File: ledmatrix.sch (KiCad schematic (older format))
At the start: 51 parts, among them U58 sled1735

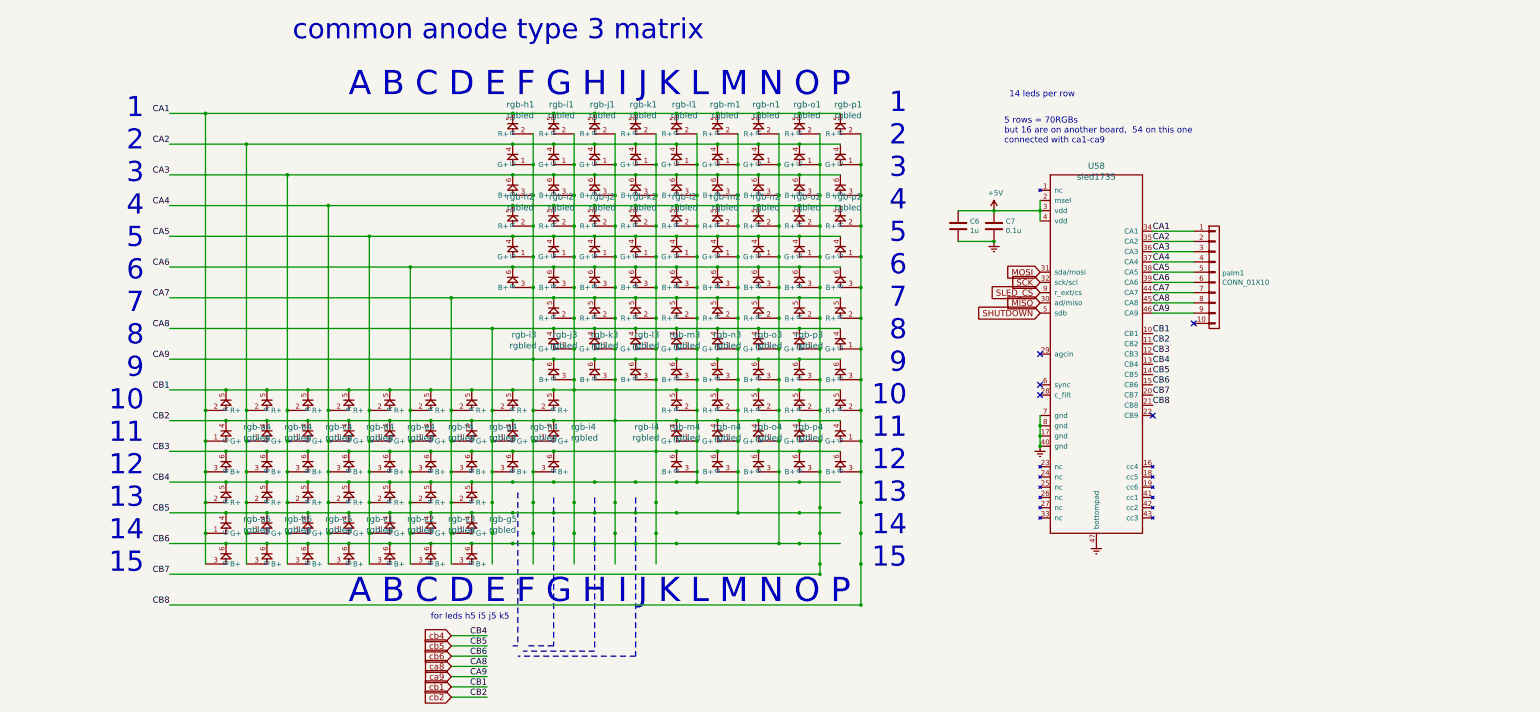
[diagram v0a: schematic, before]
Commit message: full BOM info on parts
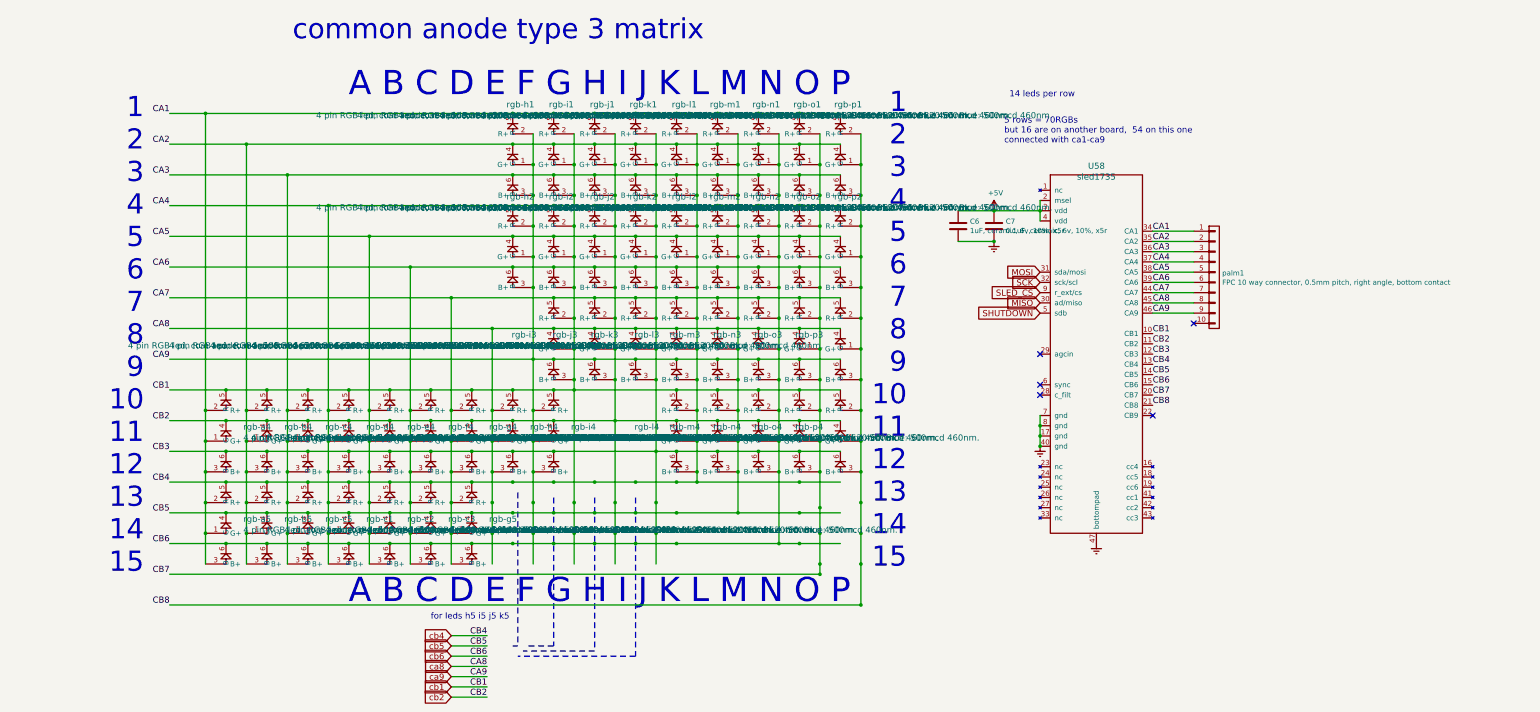
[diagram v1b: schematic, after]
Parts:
- C6: value 1u -> 1uF, ceramic, 6v, 10%, x5r; supplier (none) -> any/open
- C7: value 0.1u -> 0.1uF, ceramic, 6v, 10%, x5r; supplier (none) -> any/open
- U58: footprint fp:QFN-56_EP_4.5x6.5_Pitch0.4mm -> fp:QFN-46_EP_4.5x6.5_Pitch0.4mm; supplier (none) -> sonix; supplier PN (none) -> SLED1735
- palm1: value CONN_01X10 -> FPC 10 way connector, 0.5mm pitch, right angle, bottom contact; supplier (none) -> any/open
- rgb-a4, rgb-a5, rgb-b4, rgb-b5, rgb-c1, rgb-c2, rgb-c3, rgb-c4, rgb-c5, rgb-d4, rgb-e4, rgb-f4, rgb-g4, rgb-h1, rgb-h2, rgb-h4, rgb-i1, rgb-i2, rgb-i3, rgb-i4, rgb-j1, rgb-j2, rgb-j3, rgb-k1, rgb-k2, rgb-k3, rgb-l1, rgb-l2, rgb-l3, rgb-l4, rgb-m1, rgb-m2, rgb-m3, rgb-m4, rgb-n1, rgb-n2, rgb-n3, rgb-n4, rgb-o1, rgb-o2, rgb-o3, rgb-o4, rgb-p1, rgb-p2, rgb-p3, rgb-p4: value rgbled -> 4 pin RGB led, com anode, red: 500mcd 620nm. Green: 1000mcd 520nm. Blue: 500mcd 460nm.; supplier (none) -> any/open
- rgb-g5: value rgbled -> 4 pin RGB led, com anode, red: 500mcd 620nm. Green: 1000mcd 520nm. Blue: 500mcd 460nm.; MOQ (none) -> Value; leadtime (none) -> Value; supplier (none) -> any/open; supplier PN (none) -> Value

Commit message: changed fp name of sled and added the J to part number
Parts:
- U58: footprint fp:QFN-46_EP_4.5x6.5_Pitch0.4mm -> fp:QFN-56_EP_4.5x6.5_Pitch0.4mm; MOQ (none) -> Value; leadtime (none) -> Value; supplier PN SLED1735 -> SLED1735J
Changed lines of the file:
@@
 F 0 "U58" H 10050 2987 60  0000 C CNN
 F 1 "sled1735" H 10050 2881 60  0000 C CNN
-F 2 "fp:QFN-46_EP_4.5x6.5_Pitch0.4mm" H 9850 2250 60  0001 C CNN
+F 2 "fp:QFN-56_EP_4.5x6.5_Pitch0.4mm" H 9850 2250 60  0001 C CNN
 F 3 "" H 9850 2250 60  0001 C CNN
 F 4 "sonix" H 0   0   60  0001 C CNN "supplier"
-F 5 "SLED1735" H 0   0   60  0001 C CNN "supplier PN"
+F 5 "SLED1735J" H 0   0   60  0001 C CNN "supplier PN"
+F 6 "Value" H 9850 2250 60  0001 C CNN "MOQ"
+F 7 "Value" H 9850 2250 60  0001 C CNN "leadtime"
 	1    9850 2250
 	1    0    0    -1

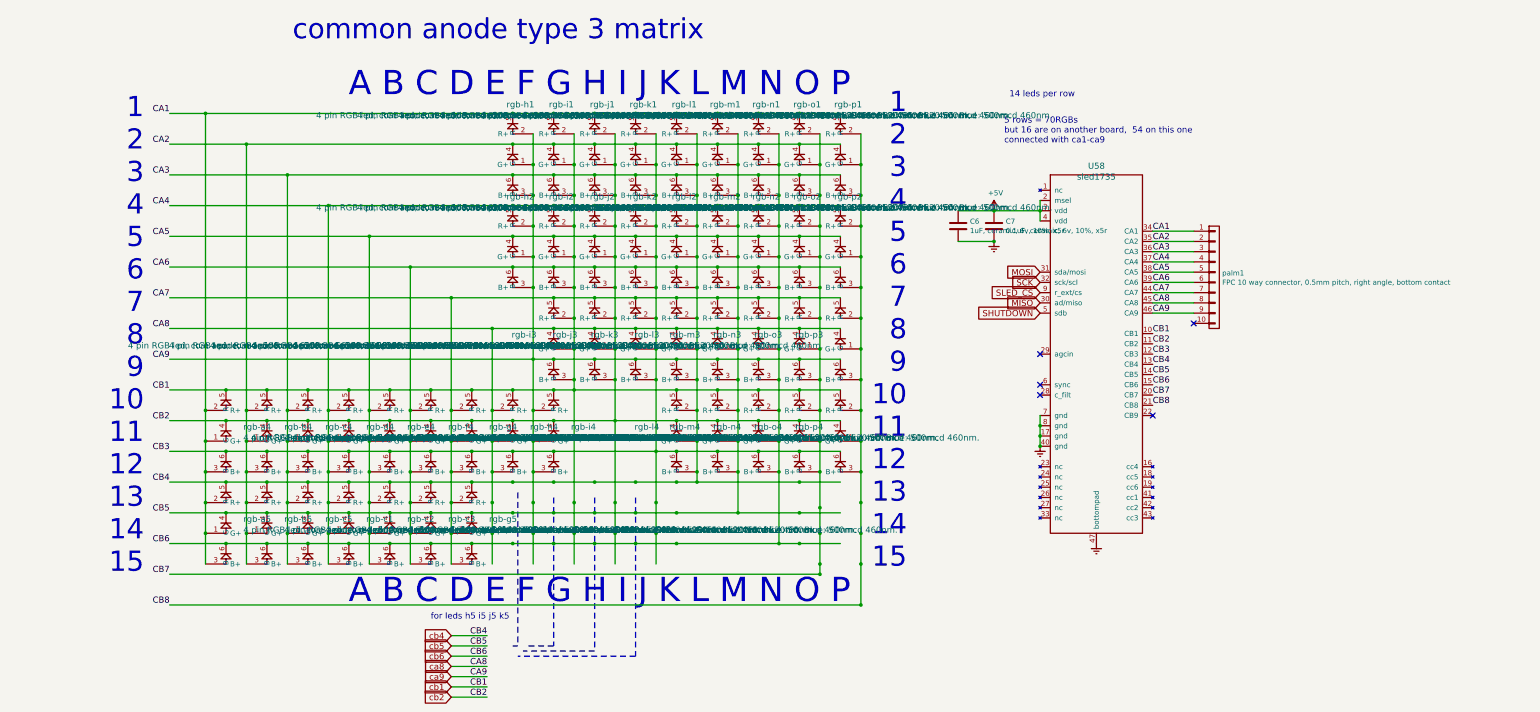
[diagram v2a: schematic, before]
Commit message: v4.4 sent to fab
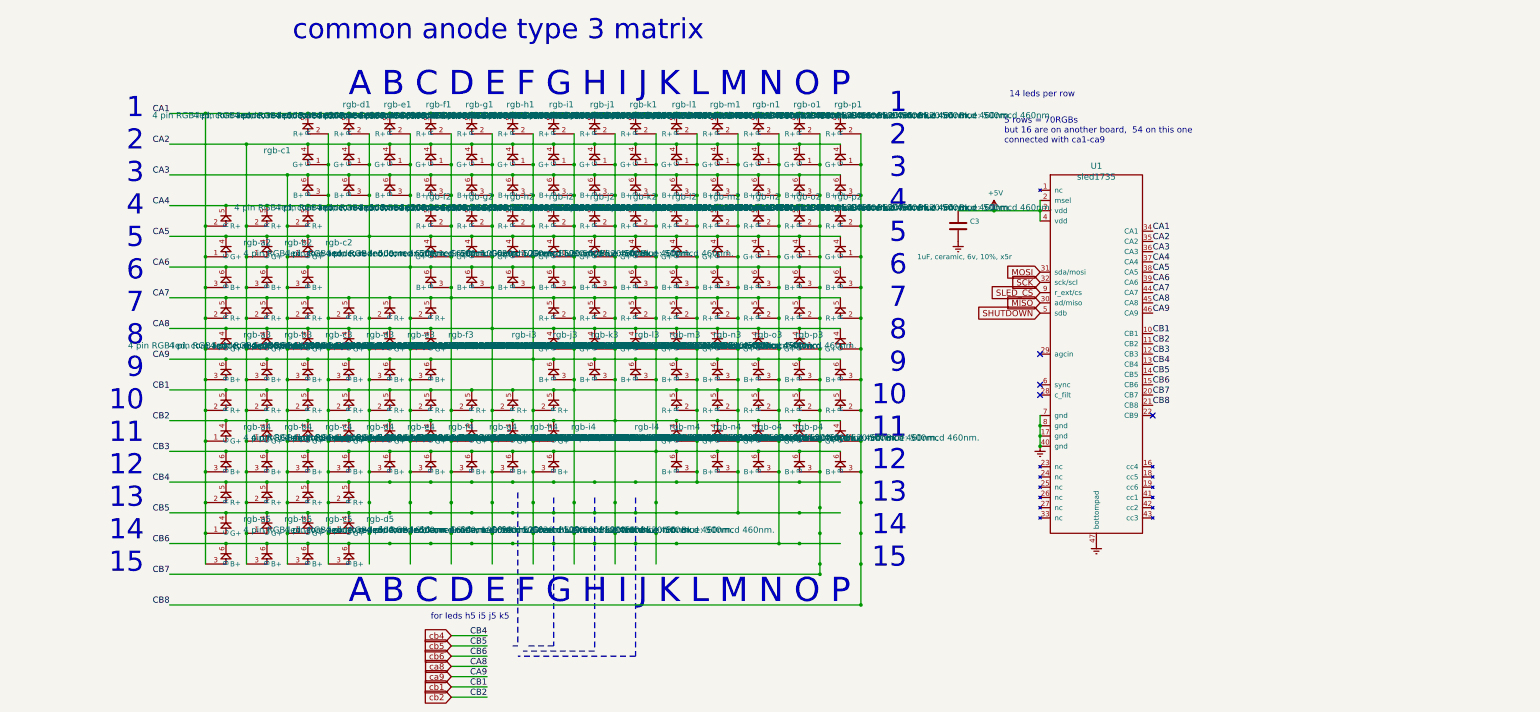
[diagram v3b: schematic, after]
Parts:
- removed C7: 0.1uF, ceramic, 6v, 10%, x5r, Capacitors_SMD:C_0805, symbol C
- removed palm1: FPC 10 way connector, 0.5mm pitch, right angle, b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, fp:FPC_10_2046, symbol CONN_01X10
- removed rgb-g5: 4 pin RGB led, com anode, red: 500mcd 620nm. Gree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, fp:3528-4p, symbol rgbled
- added rgb-a2, rgb-a3, rgb-b2, rgb-b3, rgb-c1, rgb-d1, rgb-d3, rgb-e1, rgb-e3, rgb-f1, rgb-f2, rgb-f3, rgb-g1, rgb-g2: 4 pin RGB led, com anode, red: 500mcd 620nm. Gree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, fp:3528-4p, symbol rgbled
- C3: renamed from C6; footprint Capacitors_SMD:C_0805 -> Capacitors_SMD:C_0603; MOQ (none) -> Value; leadtime (none) -> Value; supplier PN (none) -> Value
- rgb-d5: renamed from rgb-c1; MOQ (none) -> Value; leadtime (none) -> Value; supplier PN (none) -> Value
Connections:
- wire segments 54 -> 44
- no-connect marks 5 -> 4

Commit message: updated for 0603 components
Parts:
- C3: farnell # 1759422 -> 1865556
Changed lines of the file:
@@
 F 2 "Capacitors_SMD:C_0603" H 8738 1950 50  0001 C CNN
 F 3 "" H 8700 2100 50  0000 C CNN
-F 4 "1759422" H 8700 2100 60  0001 C CNN "farnell #"
+F 4 "1865556" H 8700 2100 60  0001 C CNN "farnell #"
 F 5 "any/open" H 0   0   60  0001 C CNN "supplier"
 F 6 "Value" H 8700 2100 60  0001 C CNN "supplier PN"

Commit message: text notes on leds
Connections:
- net labels removed: ca8, ca9
- wire segments 44 -> 42
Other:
- note added: "2 lights for the LP, j5 k5"
- note added: "5 rows = 70RGBs max\n2 are on low profile board"
- note removed: "5 rows = 70RGBs\nbut 16 are on another board, 54 on this one\nconnected with ca1-ca9"
- note removed: "for leds h5 i5 j5 k5"
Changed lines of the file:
@@
 14 leds per row
 Text Notes 9150 1300 0    60   ~ 0
-5 rows = 70RGBs\nbut 16 are on another board,  54 on this one\nconnected with ca1-ca9
+5 rows = 70RGBs max\n2 are on low profile board
 $Comp
 L sled1735-RESCUE-raise-left U58
@@
 Text Notes 2200 300  0    197  ~ 0
 common anode type 3 matrix
-Text Label 4100 6500 2    60   ~ 0
-CA9
 Text Label 4100 6600 2    60   ~ 0
 CB1
@@
 	4100 6300 3750 6300
 Wire Wire Line
-	3750 6500 4100 6500
-Wire Wire Line
 	4100 6600 3750 6600
 Wire Wire Line
@@
 Text Notes 750  5500 2    197  ~ 0
 1\n2\n3\n4\n5\n6\n7\n8\n9\n10\n11\n12\n13\n14\n15
-Text Notes 3550 5950 0    60   ~ 0
-for leds h5 i5 j5 k5
+Text Notes 4450 6550 0    60   ~ 0
+2 lights for the LP, j5 k5
 Text GLabel 3750 6100 0    60   Input ~ 0
 cb4
@@
 Text GLabel 3750 6300 0    60   Input ~ 0
 cb6
-Text GLabel 3750 6500 0    60   Input ~ 0
-ca9
 Text GLabel 3750 6600 0    60   Input ~ 0
 cb1
@@
 Wire Notes Line
 	5150 4750 5150 6250
-Wire Notes Line
-	5150 6250 4450 6250
-Wire Notes Line
-	4750 4750 4750 6200
-Wire Notes Line
-	4750 6200 4500 6200
-Wire Notes Line
-	4400 4700 4400 6200
-Wire Notes Line
-	4400 6200 4350 6200
-Text GLabel 3750 6400 0    60   Input ~ 0
-ca8
-Text Label 4100 6400 2    60   ~ 0
-CA8
-Wire Wire Line
-	3750 6400 4100 6400
 $Comp
 L rgbled rgb-c1

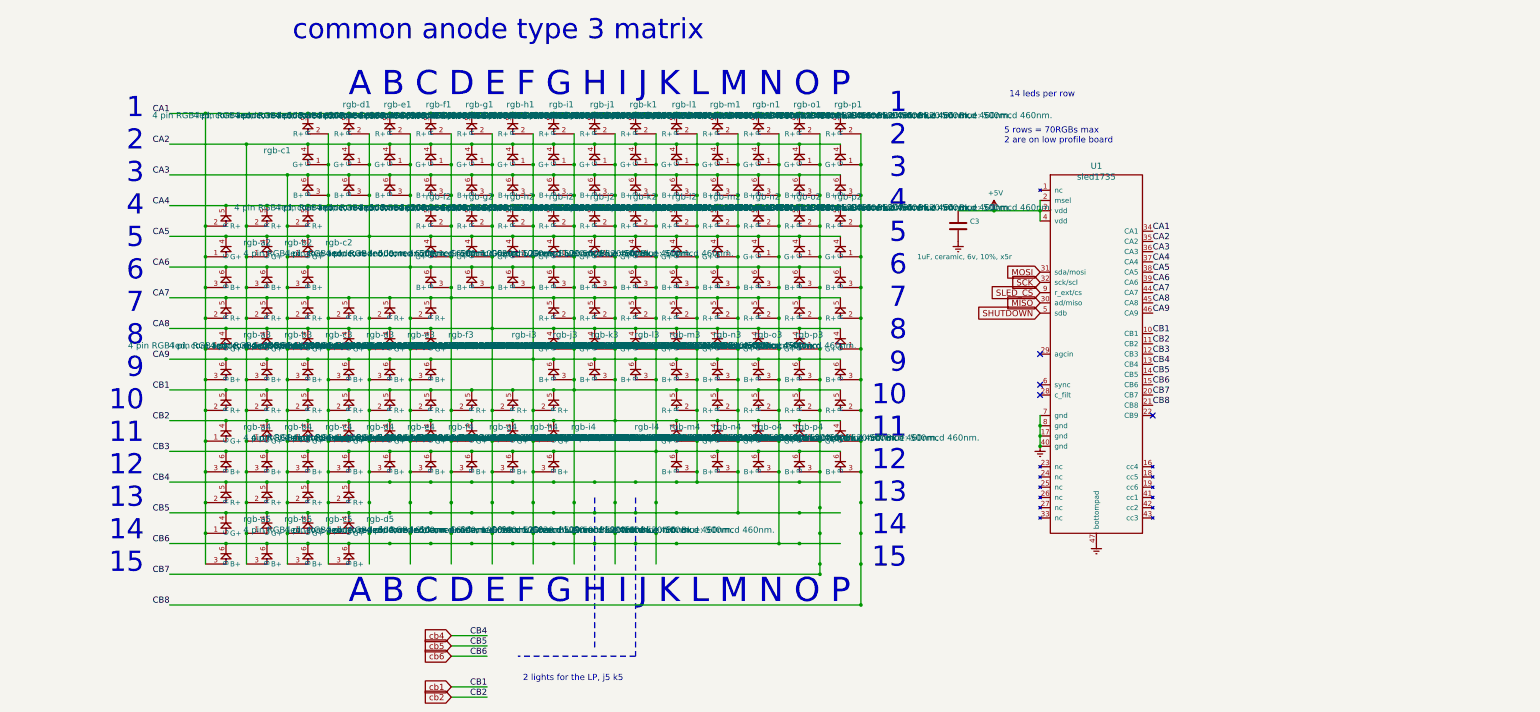
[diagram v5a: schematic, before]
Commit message: fixed ground connects on lp header, fixed broken led matrix commit that broke after 742cc9402ce5b39b1cbca2d424f676ff977e25d4
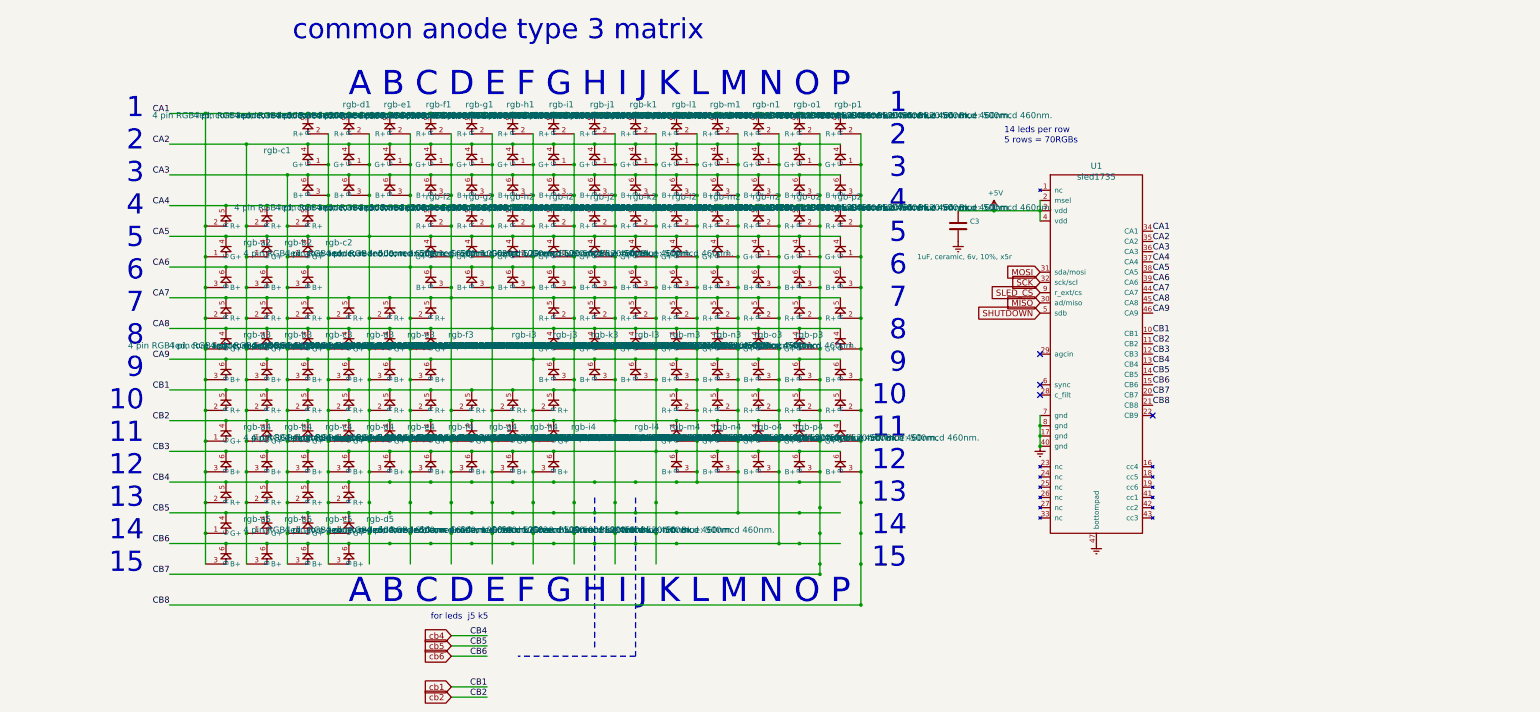
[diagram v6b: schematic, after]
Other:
- note added: "5 rows = 70RGBs\n"
- note added: "for leds j5 k5"
- note removed: "2 lights for the LP, j5 k5"
- note removed: "5 rows = 70RGBs max\n2 are on low profile board"
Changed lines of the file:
@@
 	1    0    0    -1
 $EndComp
-Text Notes 9200 850  0    60   ~ 0
+Text Notes 9150 1200 0    60   ~ 0
 14 leds per row
 Text Notes 9150 1300 0    60   ~ 0
-5 rows = 70RGBs max\n2 are on low profile board
+5 rows = 70RGBs\n
 $Comp
 L sled1735-RESCUE-raise-left U58
@@
 Text Notes 750  5500 2    197  ~ 0
 1\n2\n3\n4\n5\n6\n7\n8\n9\n10\n11\n12\n13\n14\n15
-Text Notes 4450 6550 0    60   ~ 0
-2 lights for the LP, j5 k5
+Text Notes 3550 5950 0    60   ~ 0
+for leds  j5 k5
 Text GLabel 3750 6100 0    60   Input ~ 0
 cb4

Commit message: ansi/iso work in progress
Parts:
- added rgb-ISOh2, rgb-e5: 4 pin RGB led, com anode, red: 500mcd 620nm. Gree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, fp:3528-4p, symbol rgbled
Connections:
- wire segments 42 -> 48
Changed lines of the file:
@@
 Connection ~ 2150 3600
 Connection ~ 1750 3600
+$Comp
+L rgbled rgb-e5
+U 1 1 5AE323BB
+P 3150 5100
+F 0 "rgb-e5" H 2981 5239 60  0000 R CNN
+F 1 "4 pin RGB led, com anode, red: 500mcd 620nm. Green: 1000mcd 520nm. Blue: 500mcd 460nm." H 2981 5133 60  0000 R CNN
+F 2 "fp:3528-4p" H 3150 5100 60  0001 C CNN
+F 3 "" H 3150 5100 60  0001 C CNN
+F 4 "any/open" H 400 0   60  0001 C CNN "supplier"
+F 5 "Value" H 3150 5100 60  0001 C CNN "supplier PN"
+F 6 "Value" H 3150 5100 60  0001 C CNN "MOQ"
+F 7 "Value" H 3150 5100 60  0001 C CNN "leadtime"
+	1    3150 5100
+	-1   0    0    -1
+$EndComp
+$Comp
+L rgbled rgb-ISOh2
+U 1 1 5AE32BA1
+P 4300 2450
+F 0 "rgb-ISOh2" H 4375 3037 60  0000 C CNN
+F 1 "4 pin RGB led, com anode, red: 500mcd 620nm. Green: 1000mcd 520nm. Blue: 500mcd 460nm." H 4375 2931 60  0000 C CNN
+F 2 "fp:3528-4p" H 4300 2450 60  0001 C CNN
+F 3 "" H 4300 2450 60  0001 C CNN
+F 4 "any/open" H -50 50  60  0001 C CNN "supplier"
+F 5 "Value" H 4300 2450 60  0001 C CNN "supplier PN"
+F 6 "Value" H 4300 2450 60  0001 C CNN "MOQ"
+F 7 "Value" H 4300 2450 60  0001 C CNN "leadtime"
+	1    4300 2450
+	1    0    0    -1
+$EndComp
+Wire Wire Line
+	4300 2250 4300 2200
+Connection ~ 4300 2200
+Wire Wire Line
+	4300 1950 4300 1900
+Connection ~ 4300 1900
+Wire Wire Line
+	4300 2550 4300 2500
+Connection ~ 4300 2500
+Wire Wire Line
+	4500 2450 4550 2450
+Connection ~ 4550 2450
+Wire Wire Line
+	4500 2150 4550 2150
+Connection ~ 4550 2150
+Wire Wire Line
+	4500 2750 4550 2750
+Connection ~ 4550 2750
 $EndSCHEMATC

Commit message: use local footprints
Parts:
- C3: footprint Capacitors_SMD:C_0603 -> raise_fp:C_0603
- U58: footprint fp:QFN-56_EP_4.5x6.5_Pitch0.4mm -> raise_fp:QFN-56_EP_4.5x6.5_Pitch0.4mm
- rgb-ISOh2, rgb-a2, rgb-a3, rgb-a4, rgb-a5, rgb-b2, rgb-b3, rgb-b4, rgb-b5, rgb-c1, rgb-c2, rgb-c3, rgb-c4, rgb-c5, rgb-d1, rgb-d3, rgb-d4, rgb-d5, rgb-e1, rgb-e3, rgb-e4, rgb-e5, rgb-f1, rgb-f2, rgb-f3, rgb-f4, rgb-g1, rgb-g2, rgb-g4, rgb-h1, rgb-h2, rgb-h4, rgb-i1, rgb-i2, rgb-i3, rgb-i4, rgb-j1, rgb-j2, rgb-j3, rgb-k1, rgb-k2, rgb-k3, rgb-l1, rgb-l2, rgb-l3, rgb-l4, rgb-m1, rgb-m2, rgb-m3, rgb-m4, rgb-n1, rgb-n2, rgb-n3, rgb-n4, rgb-o1, rgb-o2, rgb-o3, rgb-o4, rgb-p1, rgb-p2, rgb-p3, rgb-p4: footprint fp:3528-4p -> raise_fp:3528-4p
